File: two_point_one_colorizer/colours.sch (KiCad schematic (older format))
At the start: 25 parts, among them SW1 SW_SPDT, SW2 SW_SPDT, U5 74HC86, U8 74LS221, U9 74LS221

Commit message: update circuits
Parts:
- R23, R29: value R -> 10k
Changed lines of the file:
@@
 P 4275 1350
 F 0 "R23" H 4345 1396 50  0000 L CNN
-F 1 "R" H 4345 1305 50  0000 L CNN
+F 1 "10k" H 4345 1305 50  0000 L CNN
 F 2 "Resistor_THT:R_Axial_DIN0207_L6.3mm_D2.5mm_P7.62mm_Horizontal" V 4205 1350 50  0001 C CNN
 F 3 "~" H 4275 1350 50  0001 C CNN
@@
 P 4225 3825
 F 0 "R29" H 4295 3871 50  0000 L CNN
-F 1 "R" H 4295 3780 50  0000 L CNN
+F 1 "10k" H 4295 3780 50  0000 L CNN
 F 2 "Resistor_THT:R_Axial_DIN0207_L6.3mm_D2.5mm_P7.62mm_Horizontal" V 4155 3825 50  0001 C CNN
 F 3 "~" H 4225 3825 50  0001 C CNN

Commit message: revised all boards
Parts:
- R26, R32: value 8.2k -> (lower than) 8.2k
- RV3, RV4, RV5, RV6: value 10k -> 10k_pot
- SW1, SW2: value SW_SPDT -> SPDT
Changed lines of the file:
@@
 P 3950 1600
 F 0 "SW1" H 3950 1885 50  0000 C CNN
-F 1 "SW_SPDT" H 3950 1794 50  0000 C CNN
+F 1 "SPDT" H 3950 1794 50  0000 C CNN
 F 2 "lib_fp:mini_toggle_switch_tayda" H 3950 1600 50  0001 C CNN
 F 3 "~" H 3950 1600 50  0001 C CNN
@@
 P 6125 1200
 F 0 "RV3" H 6055 1246 50  0000 R CNN
-F 1 "10k" H 6055 1155 50  0000 R CNN
+F 1 "10k_pot" H 6055 1155 50  0000 R CNN
 F 2 "lib_fp:Potentiometer_Vertical_Large" H 6125 1200 50  0001 C CNN
 F 3 "~" H 6125 1200 50  0001 C CNN
@@
 P 8175 1200
 F 0 "RV4" H 8105 1246 50  0000 R CNN
-F 1 "10k" H 8105 1155 50  0000 R CNN
+F 1 "10k_pot" H 8105 1155 50  0000 R CNN
 F 2 "lib_fp:Potentiometer_Vertical_Large" H 8175 1200 50  0001 C CNN
 F 3 "~" H 8175 1200 50  0001 C CNN
@@
 P 3900 4075
 F 0 "SW2" H 3900 4360 50  0000 C CNN
-F 1 "SW_SPDT" H 3900 4269 50  0000 C CNN
+F 1 "SPDT" H 3900 4269 50  0000 C CNN
 F 2 "lib_fp:mini_toggle_switch_tayda" H 3900 4075 50  0001 C CNN
 F 3 "~" H 3900 4075 50  0001 C CNN
@@
 P 6075 3675
 F 0 "RV5" H 6005 3721 50  0000 R CNN
-F 1 "10k" H 6005 3630 50  0000 R CNN
+F 1 "10k_pot" H 6005 3630 50  0000 R CNN
 F 2 "lib_fp:Potentiometer_Vertical_Large" H 6075 3675 50  0001 C CNN
 F 3 "~" H 6075 3675 50  0001 C CNN
@@
 P 8125 3675
 F 0 "RV6" H 8055 3721 50  0000 R CNN
-F 1 "10k" H 8055 3630 50  0000 R CNN
+F 1 "10k_pot" H 8055 3630 50  0000 R CNN
 F 2 "lib_fp:Potentiometer_Vertical_Large" H 8125 3675 50  0001 C CNN
 F 3 "~" H 8125 3675 50  0001 C CNN
@@
 P 9450 1925
 F 0 "R26" H 9520 1971 50  0000 L CNN
-F 1 "8.2k" H 9520 1880 50  0000 L CNN
+F 1 "(lower than) 8.2k" H 9520 1880 50  0000 L CNN
 F 2 "Resistor_THT:R_Axial_DIN0207_L6.3mm_D2.5mm_P7.62mm_Horizontal" V 9380 1925 50  0001 C CNN
 F 3 "~" H 9450 1925 50  0001 C CNN
@@
 P 9400 4400
 F 0 "R32" H 9470 4446 50  0000 L CNN
-F 1 "8.2k" H 9470 4355 50  0000 L CNN
+F 1 "(lower than) 8.2k" H 9470 4355 50  0000 L CNN
 F 2 "Resistor_THT:R_Axial_DIN0207_L6.3mm_D2.5mm_P7.62mm_Horizontal" V 9330 4400 50  0001 C CNN
 F 3 "~" H 9400 4400 50  0001 C CNN

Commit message: working on nexr version for colorizer and inverter
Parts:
- added RV7, RV8: 5k_trim, lib_fp:Pot_trim_3362_tayda, symbol Device:R_POT
- R26, R32: value (lower than) 8.2k -> 1.5k
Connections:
- net +5V: now also RV7.1, RV8.1; no longer R26.1, R32.1
- new net: R26.1, RV8.2
- new net: R32.1, RV7.2
- no-connect marks 13 -> 15
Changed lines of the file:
@@
 EESchema Schematic File Version 4
-LIBS:two_point_one_colorizer-cache
 EELAYER 30 0
 EELAYER END
@@
 P 9450 1925
 F 0 "R26" H 9520 1971 50  0000 L CNN
-F 1 "(lower than) 8.2k" H 9520 1880 50  0000 L CNN
+F 1 "1.5k" H 9520 1880 50  0000 L CNN
 F 2 "Resistor_THT:R_Axial_DIN0207_L6.3mm_D2.5mm_P7.62mm_Horizontal" V 9380 1925 50  0001 C CNN
 F 3 "~" H 9450 1925 50  0001 C CNN
@@
 L power:+5V #PWR057
 U 1 1 5F26679E
-P 9450 1650
-F 0 "#PWR057" H 9450 1500 50  0001 C CNN
-F 1 "+5V" H 9465 1823 50  0000 C CNN
-F 2 "" H 9450 1650 50  0001 C CNN
-F 3 "" H 9450 1650 50  0001 C CNN
-	1    9450 1650
-	1    0    0    -1
-$EndComp
-Wire Wire Line
-	9450 1775 9450 1650
+P 9300 1350
+F 0 "#PWR057" H 9300 1200 50  0001 C CNN
+F 1 "+5V" H 9315 1523 50  0000 C CNN
+F 2 "" H 9300 1350 50  0001 C CNN
+F 3 "" H 9300 1350 50  0001 C CNN
+	1    9300 1350
+	1    0    0    -1
+$EndComp
 $Comp
 L Device:R R33
@@
 P 9400 4400
 F 0 "R32" H 9470 4446 50  0000 L CNN
-F 1 "(lower than) 8.2k" H 9470 4355 50  0000 L CNN
+F 1 "1.5k" H 9470 4355 50  0000 L CNN
 F 2 "Resistor_THT:R_Axial_DIN0207_L6.3mm_D2.5mm_P7.62mm_Horizontal" V 9330 4400 50  0001 C CNN
 F 3 "~" H 9400 4400 50  0001 C CNN
@@
 L power:+5V #PWR066
 U 1 1 5F268866
-P 9400 4125
-F 0 "#PWR066" H 9400 3975 50  0001 C CNN
-F 1 "+5V" H 9415 4298 50  0000 C CNN
-F 2 "" H 9400 4125 50  0001 C CNN
-F 3 "" H 9400 4125 50  0001 C CNN
-	1    9400 4125
-	1    0    0    -1
-$EndComp
-Wire Wire Line
-	9400 4250 9400 4125
+P 9250 3900
+F 0 "#PWR066" H 9250 3750 50  0001 C CNN
+F 1 "+5V" H 9265 4073 50  0000 C CNN
+F 2 "" H 9250 3900 50  0001 C CNN
+F 3 "" H 9250 3900 50  0001 C CNN
+	1    9250 3900
+	1    0    0    -1
+$EndComp
 Wire Wire Line
 	9450 2100 10100 2100
@@
 NoConn ~ 5550 7025
 NoConn ~ 6150 6925
+$Comp
+L Device:R_POT RV8
+U 1 1 6183AE7E
+P 9300 1500
+F 0 "RV8" H 9230 1546 50  0000 R CNN
+F 1 "5k_trim" H 9230 1455 50  0000 R CNN
+F 2 "lib_fp:Pot_trim_3362_tayda" H 9300 1500 50  0001 C CNN
+F 3 "~" H 9300 1500 50  0001 C CNN
+	1    9300 1500
+	1    0    0    -1
+$EndComp
+NoConn ~ 9300 1650
+Wire Wire Line
+	9450 1500 9450 1775
+$Comp
+L Device:R_POT RV7
+U 1 1 61847C8C
+P 9250 4050
+F 0 "RV7" H 9180 4096 50  0000 R CNN
+F 1 "5k_trim" H 9180 4005 50  0000 R CNN
+F 2 "lib_fp:Pot_trim_3362_tayda" H 9250 4050 50  0001 C CNN
+F 3 "~" H 9250 4050 50  0001 C CNN
+	1    9250 4050
+	1    0    0    -1
+$EndComp
+Wire Wire Line
+	9400 4050 9400 4250
+NoConn ~ 9250 4200
 $EndSCHEMATC

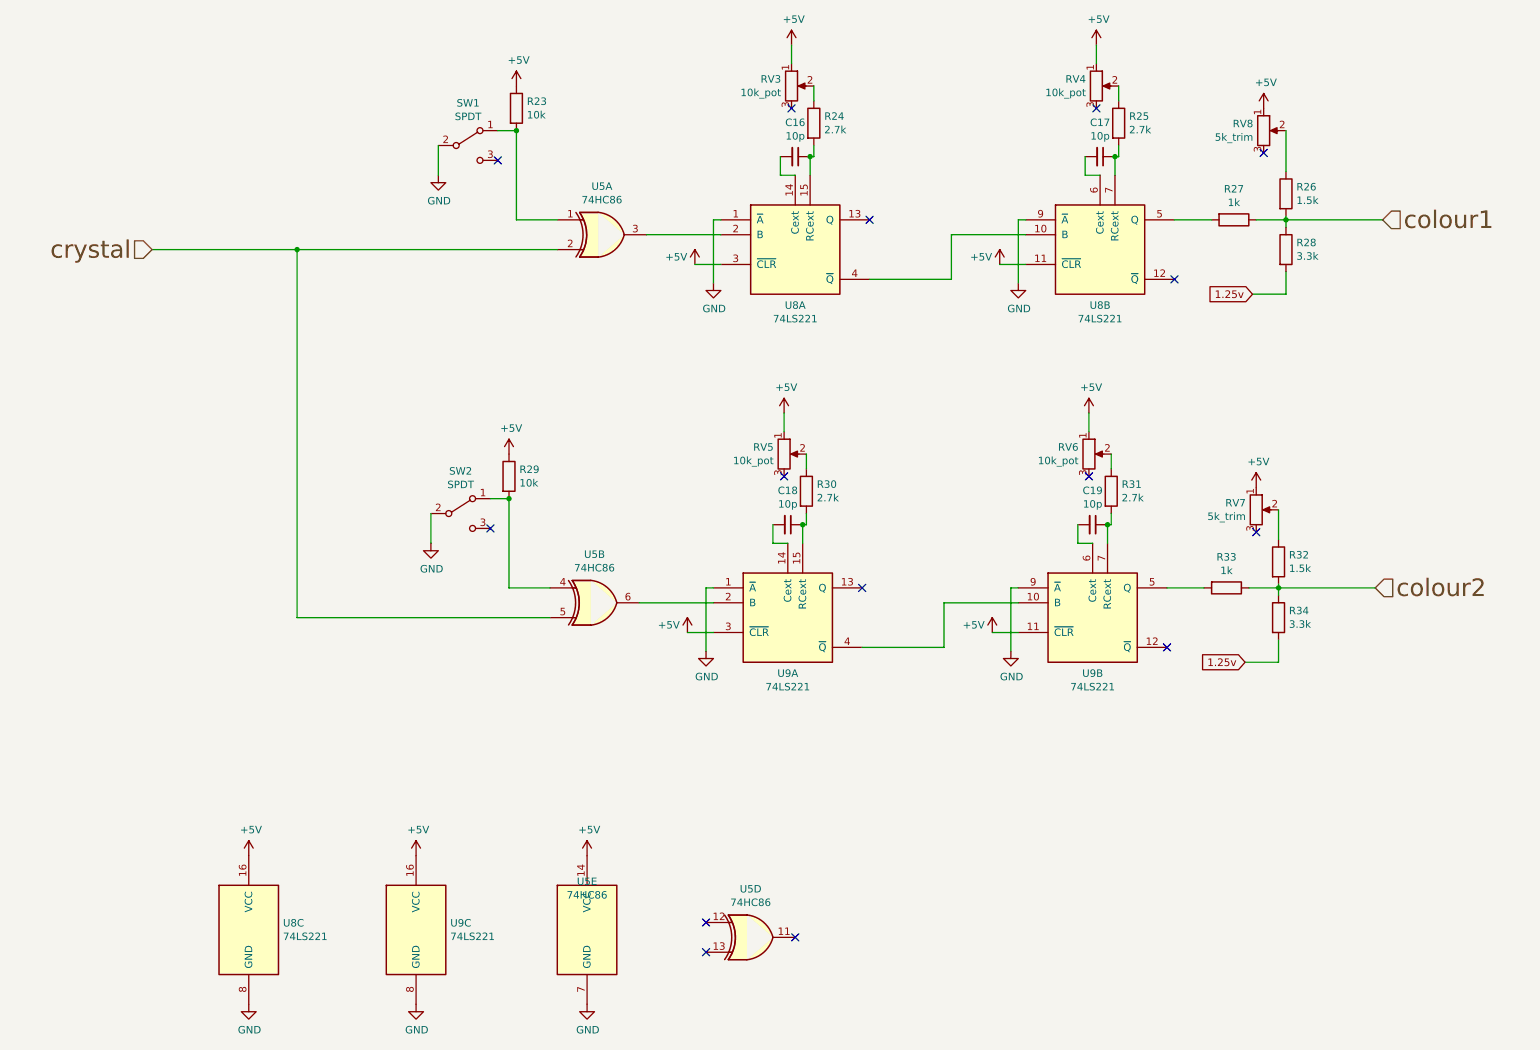
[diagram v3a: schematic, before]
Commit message: lay out colorizer
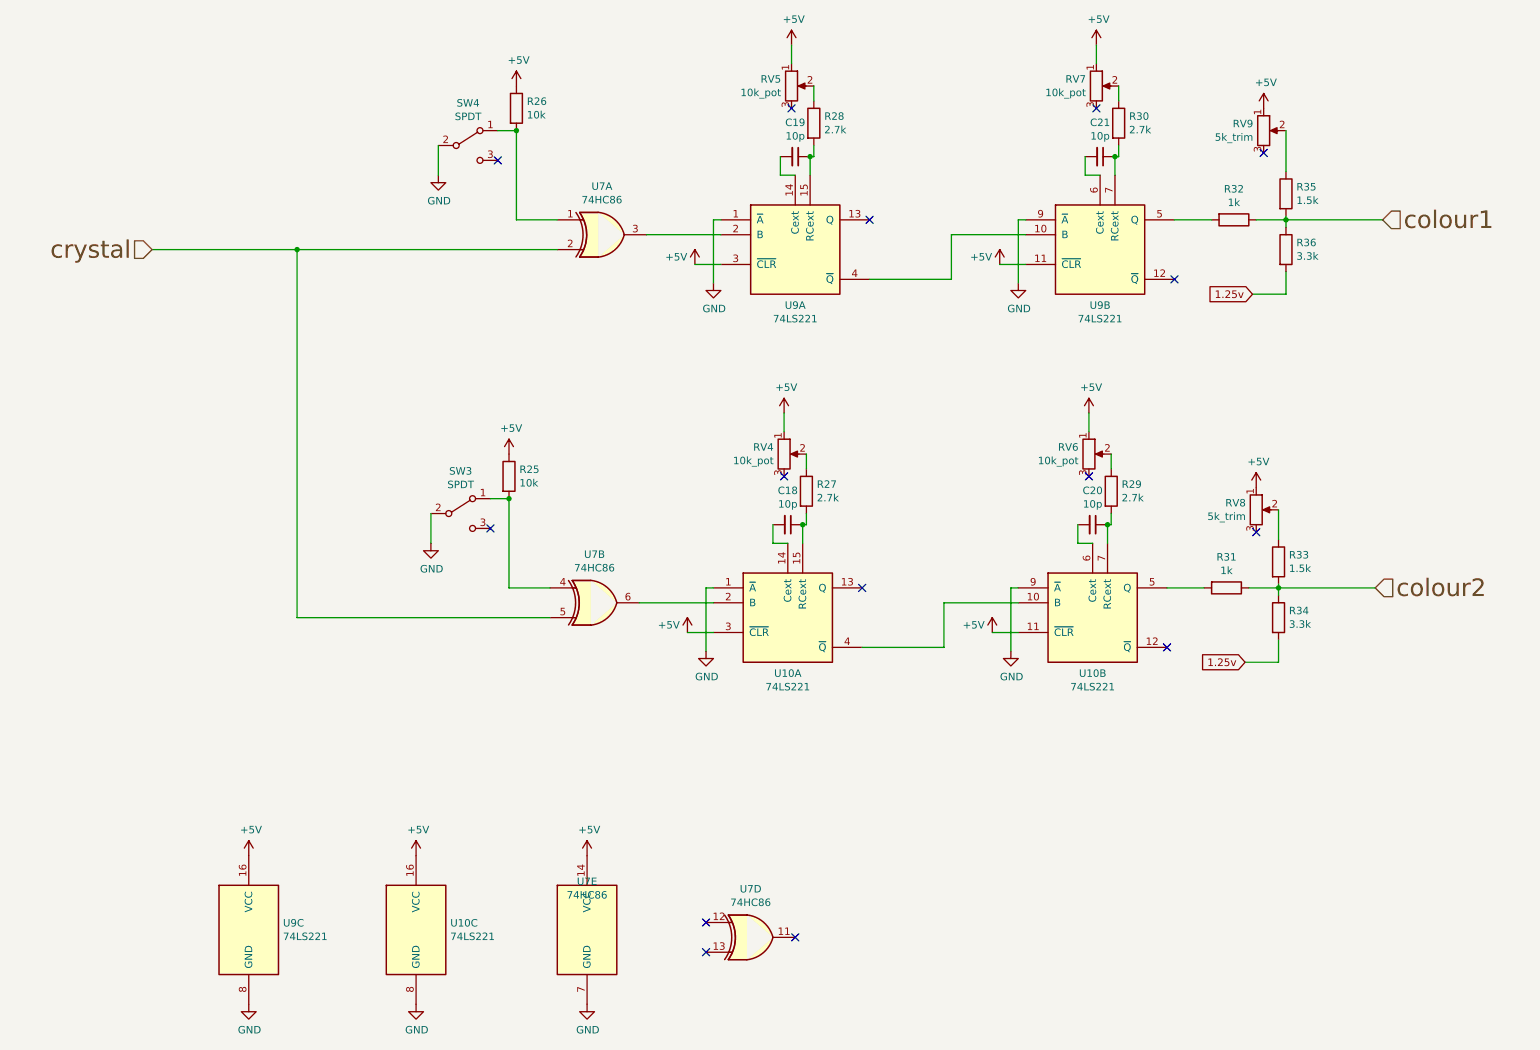
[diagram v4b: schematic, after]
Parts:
- C18: footprint Capacitor_THT:C_Disc_D4.7mm_W2.5mm_P5.00mm -> lib_fp:C_Disc_D4.7mm_W2.5mm_P5.00mm
- C19: renamed from C16; footprint Capacitor_THT:C_Disc_D4.7mm_W2.5mm_P5.00mm -> lib_fp:C_Disc_D4.7mm_W2.5mm_P5.00mm
- C20: renamed from C19; footprint Capacitor_THT:C_Disc_D4.7mm_W2.5mm_P5.00mm -> lib_fp:C_Disc_D4.7mm_W2.5mm_P5.00mm
- C21: renamed from C17; footprint Capacitor_THT:C_Disc_D4.7mm_W2.5mm_P5.00mm -> lib_fp:C_Disc_D4.7mm_W2.5mm_P5.00mm
- R25: renamed from R29; footprint Resistor_THT:R_Axial_DIN0207_L6.3mm_D2.5mm_P7.62mm_Horizontal -> lib_fp:R_Axial_DIN0207_L6.3mm_D2.5mm_P7.62mm_Horizontal
- R26: renamed from R23; footprint Resistor_THT:R_Axial_DIN0207_L6.3mm_D2.5mm_P7.62mm_Horizontal -> lib_fp:R_Axial_DIN0207_L6.3mm_D2.5mm_P7.62mm_Horizontal
- R27: renamed from R30; footprint Resistor_THT:R_Axial_DIN0207_L6.3mm_D2.5mm_P7.62mm_Horizontal -> lib_fp:R_Axial_DIN0207_L6.3mm_D2.5mm_P7.62mm_Horizontal
- R28: renamed from R24; footprint Resistor_THT:R_Axial_DIN0207_L6.3mm_D2.5mm_P7.62mm_Horizontal -> lib_fp:R_Axial_DIN0207_L6.3mm_D2.5mm_P7.62mm_Horizontal
- R29: renamed from R31; footprint Resistor_THT:R_Axial_DIN0207_L6.3mm_D2.5mm_P7.62mm_Horizontal -> lib_fp:R_Axial_DIN0207_L6.3mm_D2.5mm_P7.62mm_Horizontal
- R30: renamed from R25; footprint Resistor_THT:R_Axial_DIN0207_L6.3mm_D2.5mm_P7.62mm_Horizontal -> lib_fp:R_Axial_DIN0207_L6.3mm_D2.5mm_P7.62mm_Horizontal
- R31: renamed from R33; footprint Resistor_THT:R_Axial_DIN0207_L6.3mm_D2.5mm_P7.62mm_Horizontal -> lib_fp:R_Axial_DIN0207_L6.3mm_D2.5mm_P7.62mm_Horizontal
- R32: renamed from R27; footprint Resistor_THT:R_Axial_DIN0207_L6.3mm_D2.5mm_P7.62mm_Horizontal -> lib_fp:R_Axial_DIN0207_L6.3mm_D2.5mm_P7.62mm_Horizontal
- R33: renamed from R32; footprint Resistor_THT:R_Axial_DIN0207_L6.3mm_D2.5mm_P7.62mm_Horizontal -> lib_fp:R_Axial_DIN0207_L6.3mm_D2.5mm_P7.62mm_Horizontal
- R34: footprint Resistor_THT:R_Axial_DIN0207_L6.3mm_D2.5mm_P7.62mm_Horizontal -> lib_fp:R_Axial_DIN0207_L6.3mm_D2.5mm_P7.62mm_Horizontal
- R35: renamed from R26; footprint Resistor_THT:R_Axial_DIN0207_L6.3mm_D2.5mm_P7.62mm_Horizontal -> lib_fp:R_Axial_DIN0207_L6.3mm_D2.5mm_P7.62mm_Horizontal
- R36: renamed from R28; footprint Resistor_THT:R_Axial_DIN0207_L6.3mm_D2.5mm_P7.62mm_Horizontal -> lib_fp:R_Axial_DIN0207_L6.3mm_D2.5mm_P7.62mm_Horizontal
- renumbered RV5 to RV4, RV3 to RV5, RV4 to RV7, RV7 to RV8, RV8 to RV9, SW2 to SW3, SW1 to SW4, U9 to U10, U5 to U7, U8 to U9
